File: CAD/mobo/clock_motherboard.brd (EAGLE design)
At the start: 68.6 x 53.3 mm, 32 parts, among them IC1 LM1086CT-5.0, IC2 LM1086CT-3.3, J2 2.1MMJACK, U1 ATMEGA328P_PDIP, U2 DS1307, Y2 32.768

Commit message: Updating motherboard CAD files (OSHpark version)
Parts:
- added GND: (no value), SparkFun-Connectors:1X06_NO_SILK
- added RDIV: 10K, rcl-ez:0207/5V
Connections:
- net A0: now also RDIV.2
- net GND: now also GND.1, GND.2, GND.3, GND.4, GND.5, GND.6, JP4.3; no longer JP4.1
- net VCC: now also RDIV.1
- net VIN: now also JP4.1; no longer JP4.3
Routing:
- net VCC: track 162.3 -> 168.7 mm
- net VIN: track 118.9 -> 113.4 mm
- net A0: track 9.65 -> 12.9 mm
- net D11/MOSI: track 90.1 -> 92.5 mm
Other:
- board size 68.6 x 53.3 mm -> 69.3 x 55.1 mm
- board text added: "GND"
- board text added: "VCC"
- board text added: "VIN"

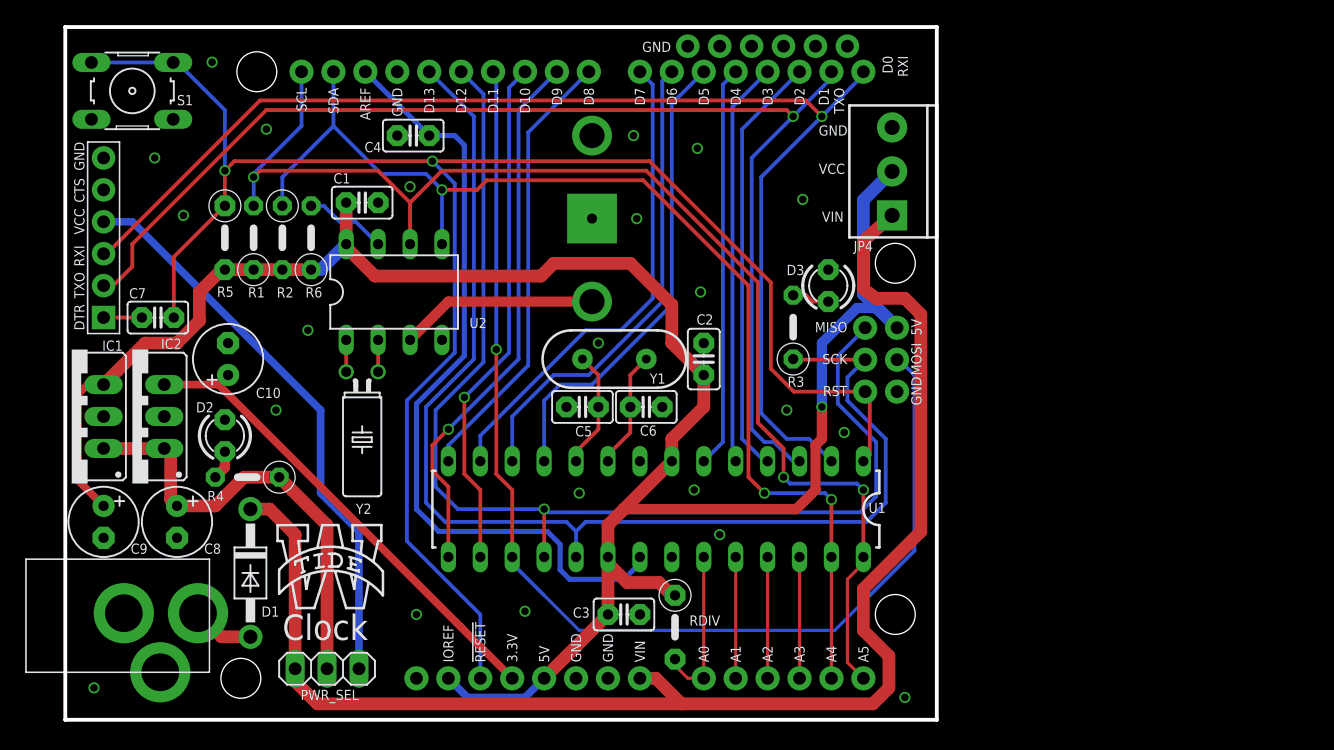
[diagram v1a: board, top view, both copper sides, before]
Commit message: Adding updated part database and motherboard BOM, closes #4
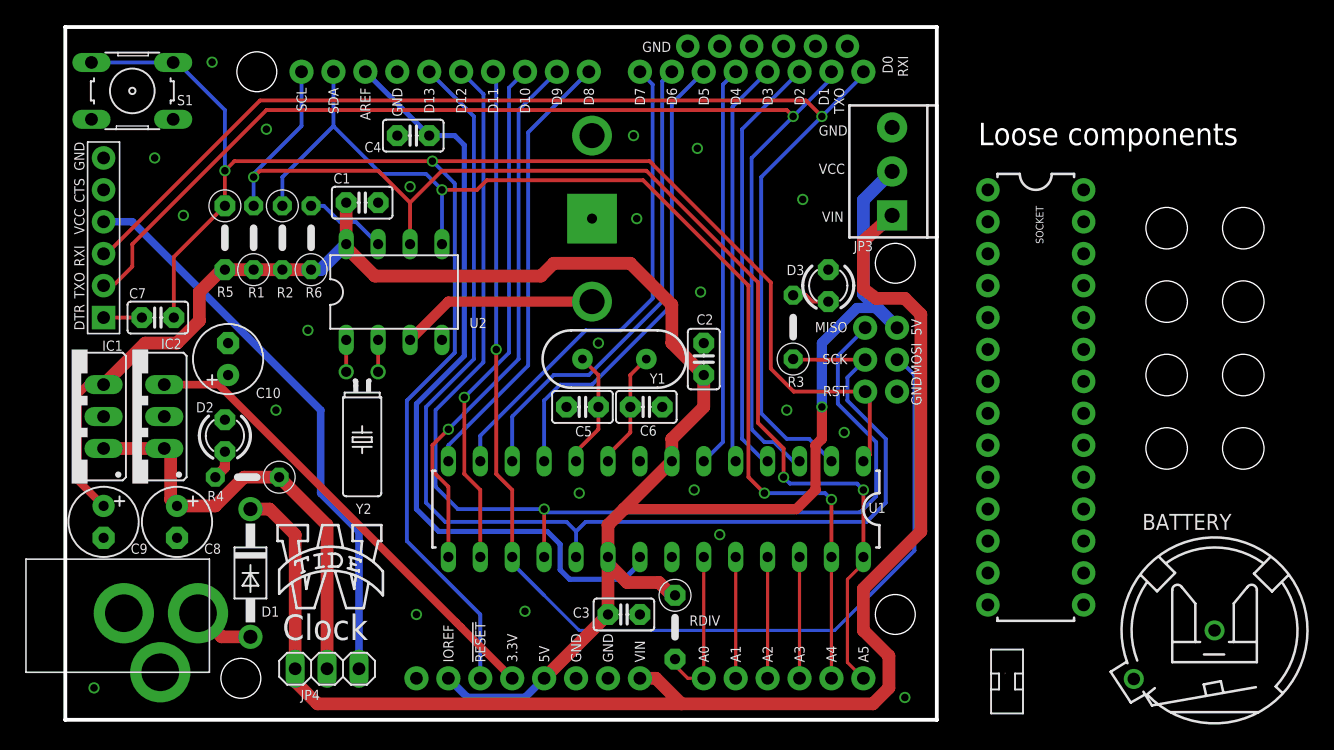
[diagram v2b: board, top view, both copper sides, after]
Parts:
- removed PWR_SEL: (no value), pinhead:1X03
- added BATTERY: CH23-1220LF, battery:CH23-1220LF
- added J1: 2.1MMJACK, minimidi:PJ-102A
- added JP3: PWR_OUT, SparkFun-Connectors:SCREWTERMINAL-3.5MM-3
- added SOCKET: ZIFSOCKET-28-3ZIFFSOCKET-28-3, SparkFun-Connectors:DIL28-3-ZIF_SOCKET
- added STANDOFF1, STANDOFF2, STANDOFF3, STANDOFF4, STANDOFF5, STANDOFF6, STANDOFF7, STANDOFF8: STAND-OFF, SparkFun-Electromechanical:STAND-OFF
- C10, C9: value 100/6VuF -> 50uF/6V
- D2: value (none) -> RED
- D3: value (none) -> YELLOW
- J2: value 2.1MMJACK -> PWR_SEL; device minimidi:PJ-102A -> jumper:JUMP
- JP4: value (none) -> PWR_SEL; device SparkFun-Connectors:SCREWTERMINAL-3.5MM-3 -> pinhead:1X03
- Y1: value (none) -> 16MHz
- moved J2 73.9 mm to (74.9, 2.29), turned to 0 degrees
- moved JP4 57.6 mm to (20.8, 3.30), turned to 180 degrees
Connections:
- net FTDI_VCC: now also JP4.1; no longer PWR_SEL.1
- net GND: now also J1.RING, JP3.3; no longer J2.RING, JP4.3
- net N$17: now also J1.TIP; no longer J2.TIP
- net PWR: now also JP4.2; no longer PWR_SEL.2
- net VCC: now also JP3.2; no longer JP4.2
- net VIN: now also JP3.1, JP4.3; no longer JP4.1, PWR_SEL.3
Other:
- board text added: "Loose components"

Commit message: Fixed mobo power circuit and updated BOM
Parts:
- C10: value 50uF/6V -> 10uF/6V
- C8: value 22uF/25V -> 0.22uF/25V
- C9: value 50uF/6V -> 0.1uF/6V
- IC1: value LM1086CT-5.0 -> LM7805CT
- IC2: value LM1086CT-3.3 -> LM2937ET-3.3
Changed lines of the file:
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@@
 <attribute name="OC_NEWARK" value="36M3542" x="5.334" y="49.276" size="1.778" layer="27" rot="R180" display="off"/>
 </element>
-<element name="IC2" library="v-reg" package="78XXS" value="LM1086CT-3.3" x="5.334" y="23.368" smashed="yes" rot="R90">
+<element name="IC2" library="v-reg" package="78XXS" value="LM2937ET-3.3" x="5.334" y="23.368" smashed="yes" rot="R90">
 <attribute name="NAME" x="7.62" y="28.7528" size="0.8128" layer="25" ratio="10"/>
 <attribute name="VALUE" x="12.954" y="18.288" size="1.27" layer="27" ratio="10" rot="R90"/>
-<attribute name="PARTNO" value="LM1086CT-3.3/NOPB" x="5.334" y="23.368" size="1.778" layer="27" rot="R90" display="off"/>
+<attribute name="PARTNO" value="LM2937ET-3.3/NOPB" x="5.334" y="23.368" size="1.778" layer="27" rot="R90" display="off"/>
 </element>
-<element name="IC1" library="v-reg" package="78XXS" value="LM1086CT-5.0" x="0.508" y="23.368" smashed="yes" rot="R90">
+<element name="IC1" library="v-reg" package="78XXS" value="LM7805CT" x="0.508" y="23.368" smashed="yes" rot="R90">
 <attribute name="NAME" x="4.572" y="29.4132" size="0.8128" layer="25" ratio="10" rot="R180"/>
 <attribute name="VALUE" x="8.128" y="18.288" size="1.27" layer="27" ratio="10" rot="R90"/>
-<attribute name="PARTNO" value="LM1086CT-5.0/NOPB" x="0.508" y="23.368" size="1.778" layer="27" rot="R90" display="off"/>
+<attribute name="PARTNO" value="LM7805CT/NOPB" x="0.508" y="23.368" size="1.778" layer="27" rot="R90" display="off"/>
 </element>
 <element name="J1" library="minimidi" package="PJ-102A" value="2.1MMJACK" x="1.27" y="7.62" rot="R90">
@@
 <attribute name="PARTNO" value="CFR-25JB-52-1K" x="14.478" y="18.542" size="1.778" layer="27" rot="R180" display="off"/>
 </element>
-<element name="C10" library="minimidi" package="E2,5-6" value="50uF/6V" x="12.954" y="27.94" smashed="yes" rot="R90">
+<element name="C10" library="minimidi" package="E2,5-6" value="10uF/6V" x="12.954" y="27.94" smashed="yes" rot="R90">
 <attribute name="NAME" x="17.145" y="25.654" size="0.8128" layer="25" ratio="10" rot="R180"/>
 <attribute name="VALUE" x="15.621" y="30.607" size="1.27" layer="27" ratio="10" rot="R90"/>
-<attribute name="PARTNO" value="ECA-1CM470I" x="12.954" y="27.94" size="1.778" layer="27" rot="R90" display="off"/>
+<attribute name="PARTNO" value="A758BG106M1EAAE070" x="12.954" y="27.94" size="1.778" layer="27" rot="R90" display="off"/>
 </element>
 <element name="JP4" library="pinhead" package="1X03" value="PWR_SEL" x="20.828" y="3.302" smashed="yes" rot="R180">
@@
 <attribute name="PARTNO" value="68001-403HLF" x="20.828" y="3.302" size="1.778" layer="27" rot="R180" display="off"/>
 </element>
-<element name="C9" library="minimidi" package="E2,5-6" value="50uF/6V" x="3.048" y="14.986" smashed="yes" rot="R270">
+<element name="C9" library="minimidi" package="E2,5-6" value="0.1uF/6V" x="3.048" y="14.986" smashed="yes" rot="R270">
 <attribute name="NAME" x="5.207" y="12.446" size="0.8128" layer="25" ratio="10"/>
 <attribute name="VALUE" x="0.381" y="12.319" size="1.27" layer="27" ratio="10" rot="R270"/>
-<attribute name="PARTNO" value="ECA-1CM470I" x="3.048" y="14.986" size="1.778" layer="27" rot="R270" display="off"/>
+<attribute name="PARTNO" value="21RZ310-RC" x="3.048" y="14.986" size="1.778" layer="27" rot="R270" display="off"/>
 </element>
 <element name="R1" library="minimidi" package="0207/5V" value="4.7 K" x="14.986" y="37.592" smashed="yes" rot="R90">
@@
 <attribute name="PARTNO" value="CFR-25JB-52-1K" x="57.912" y="30.48" size="1.778" layer="27" rot="R90" display="off"/>
 </element>
-<element name="C8" library="minimidi" package="E2,5-6" value="22uF/25V" x="8.89" y="14.986" smashed="yes" rot="R270">
+<element name="C8" library="minimidi" package="E2,5-6" value="0.22uF/25V" x="8.89" y="14.986" smashed="yes" rot="R270">
 <attribute name="NAME" x="11.049" y="12.446" size="0.8128" layer="25" ratio="10"/>
 <attribute name="VALUE" x="6.223" y="12.319" size="1.27" layer="27" ratio="10" rot="R270"/>
-<attribute name="PARTNO" value="EEU-FR1H220B" x="8.89" y="14.986" size="1.778" layer="27" rot="R270" display="off"/>
+<attribute name="PARTNO" value="FG14X7R1H224KNT06" x="8.89" y="14.986" size="1.778" layer="27" rot="R270" display="off"/>
 </element>
 <element name="JP2" library="clock_motherboard" package="FTDI_DEVICE_SIDE" value="FTDI_DEVICE" x="3.048" y="37.592" rot="R90">
